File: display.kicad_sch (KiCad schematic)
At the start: 33 parts, among them J701 Socket_Molex_SlimStack_2x15_5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, J702 HDMI-A_WE_685119134923

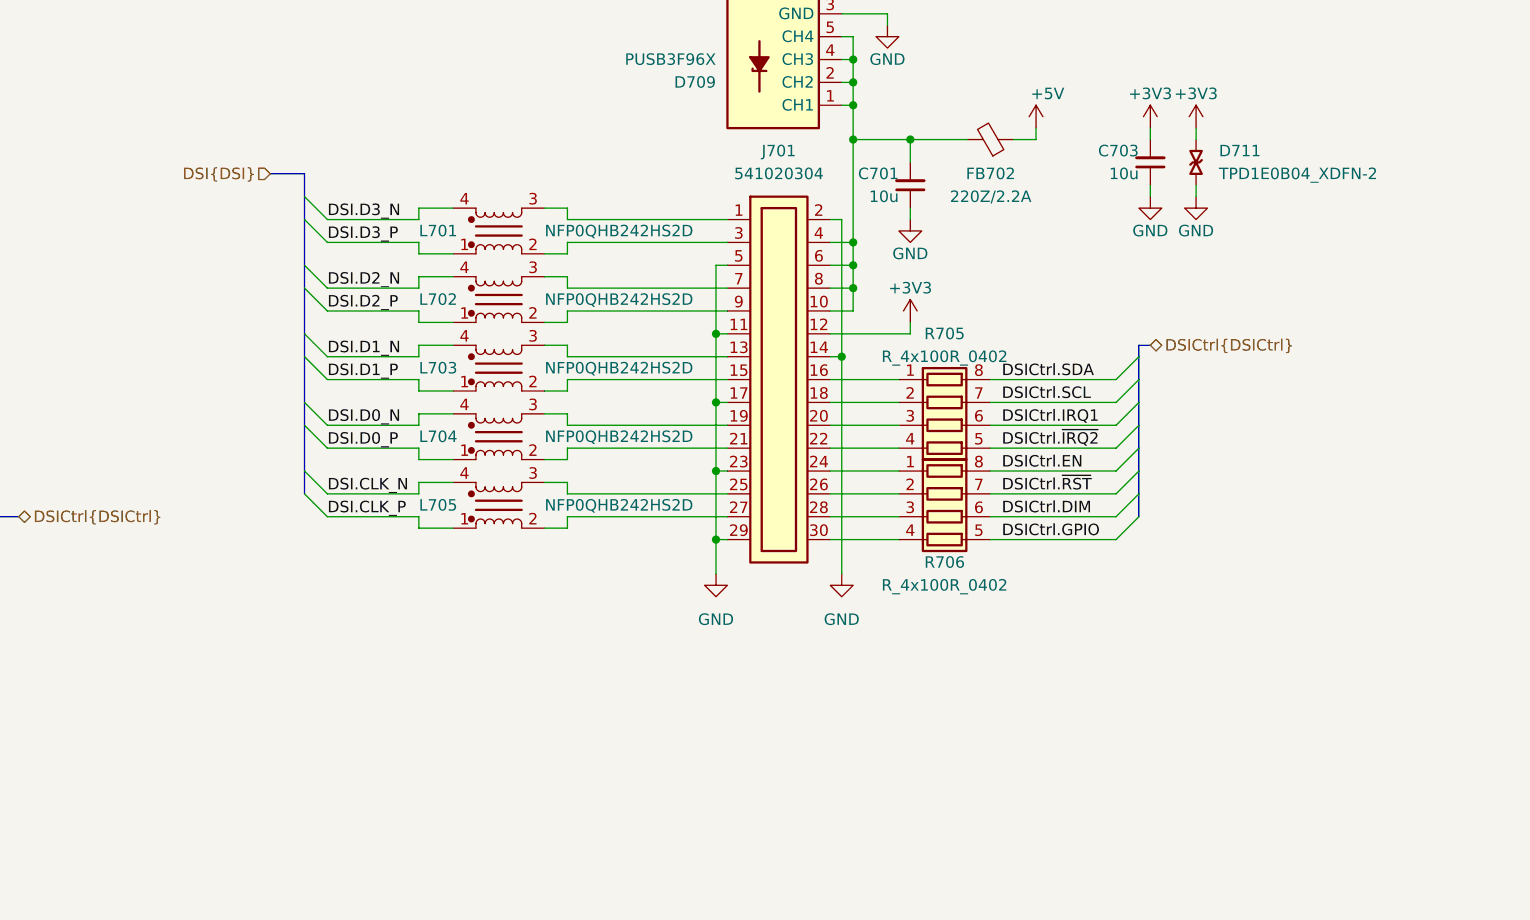
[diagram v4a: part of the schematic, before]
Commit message: [#54932] Change adapter connector (from 2x15 to 2x20)
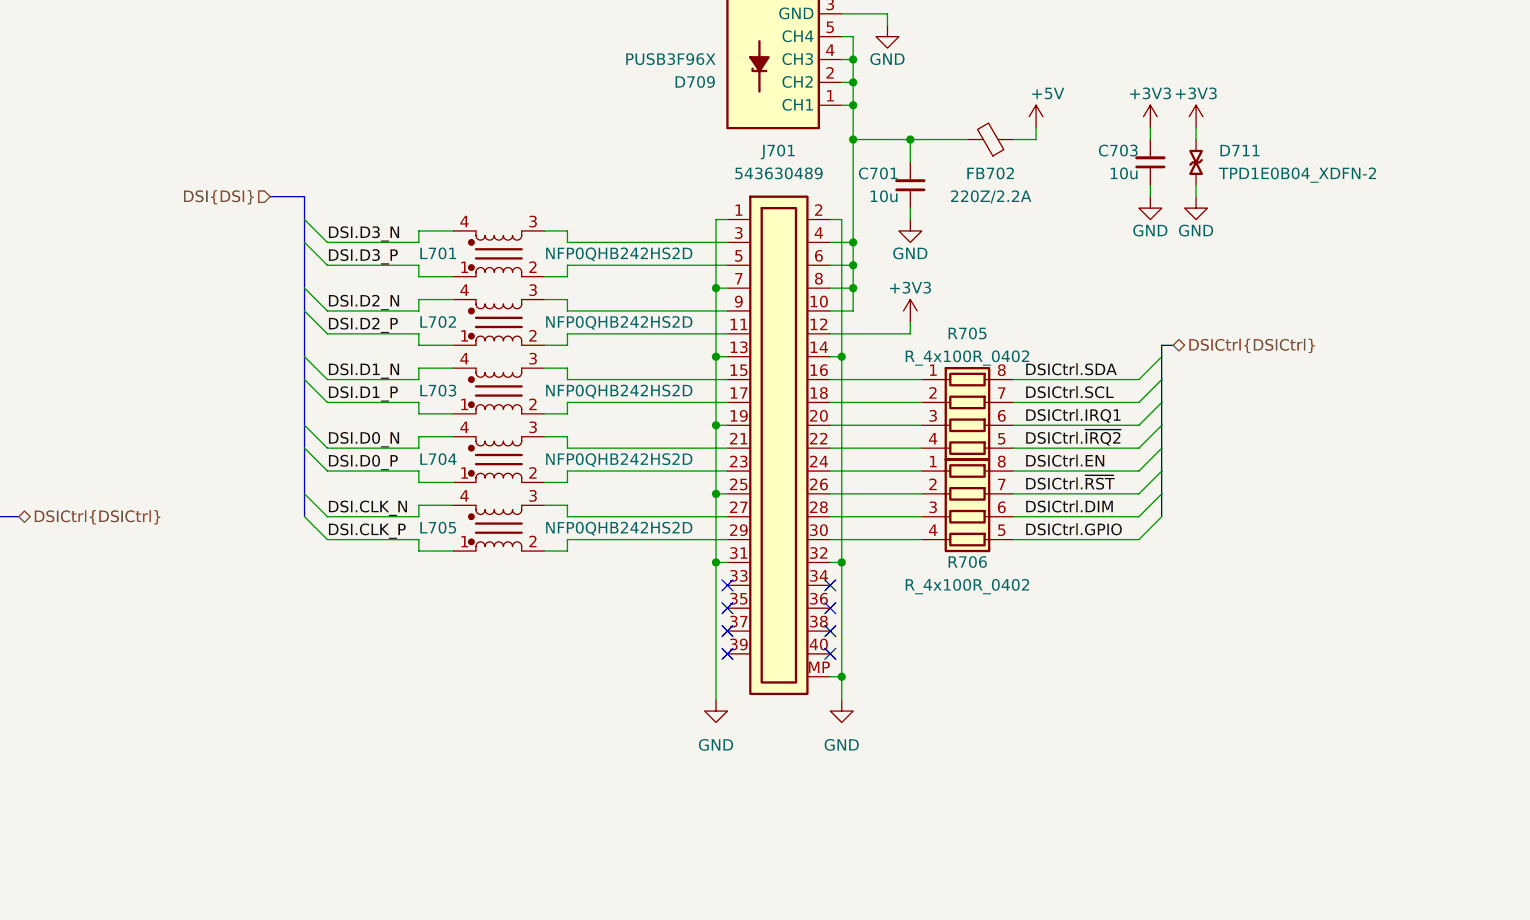
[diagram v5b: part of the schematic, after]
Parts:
- J701: value Socket_Molex_SlimStack_2x15_541020304 -> Socket_Molex_SlimStack_2x20_543630489; footprint antmicro-footprints:Conn_Socket_Molex_SlimStack_2x15_541020304 -> antmicro-footprints:Conn_Socket_Molex_SlimStack_2x20_543630489; symbol antmicroB2BConnectors:Socket_Molex_SlimStack_2x15_541020304 -> antmicroB2BConnectors:Socket_Molex_SlimStack_2x20_543630489; MPN 541020304 -> 543630489
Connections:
- net GND: now also J701.1, J701.13, J701.19, J701.25, J701.31, J701.32, J701.7, J701.MP; no longer J701.11, J701.17, J701.23, J701.29, J701.5
- net at L701.3: now also J701.3; no longer J701.1
- net at L703.3: now also J701.15; no longer J701.13
- net at L703.2: now also J701.17; no longer J701.15
- net at L704.3: now also J701.21; no longer J701.19
- net at L704.2: now also J701.23; no longer J701.21
- net at L705.3: now also J701.27; no longer J701.25
- net at L705.2: now also J701.29; no longer J701.27
- net at L701.2: now also J701.5; no longer J701.3
- net at L702.3: now also J701.9; no longer J701.7
- net at L702.2: now also J701.11; no longer J701.9
- no-connect marks 1 -> 9
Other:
- moved on the sheet: L701, L702, L703, L704, L705, R705, R706

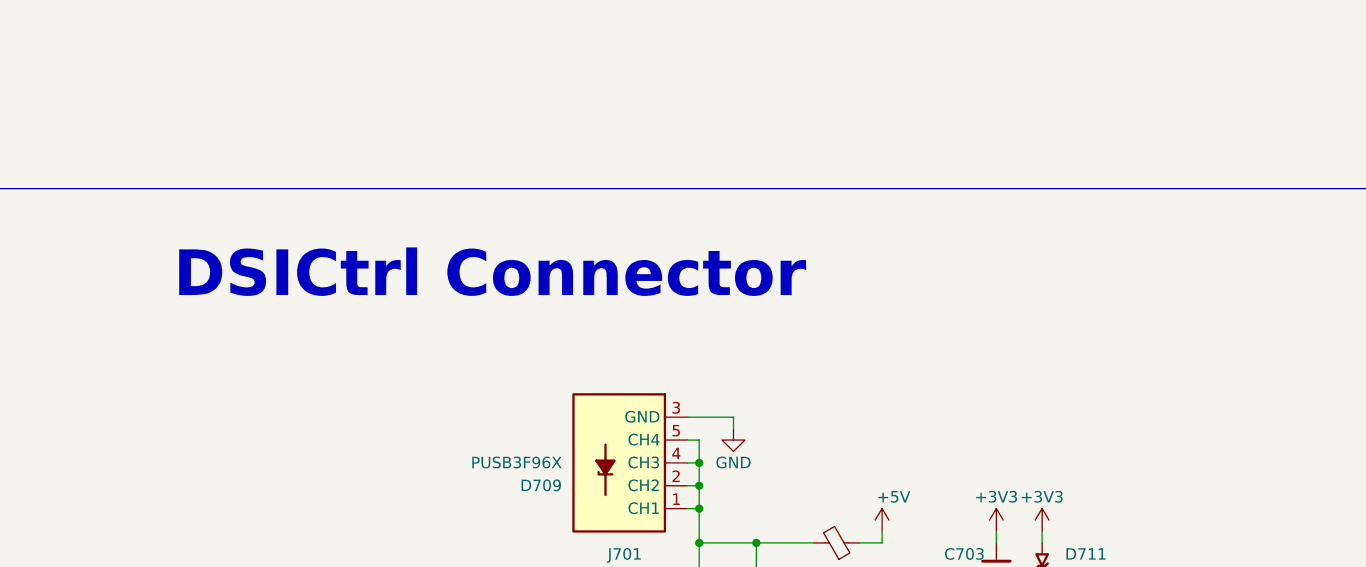
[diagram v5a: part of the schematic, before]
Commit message: [#54617] Change level shifter for I2C
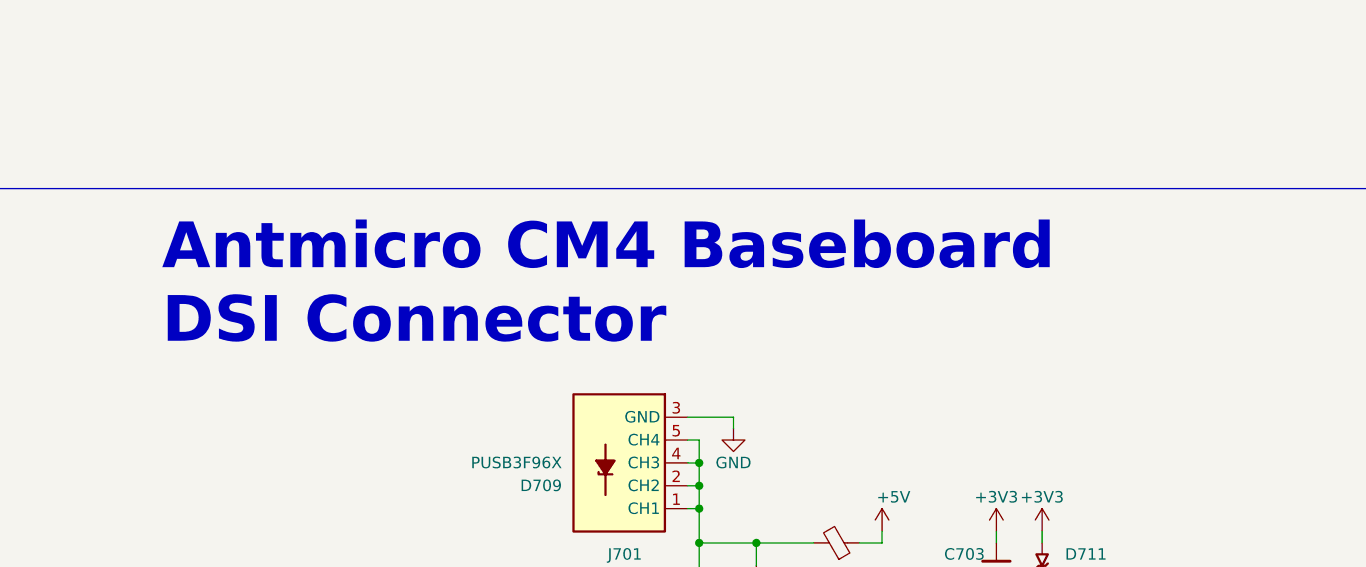
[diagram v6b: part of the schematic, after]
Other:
- note added: "Antmicro CM4 Baseboard DSI Connector"
- note removed: "DSICtrl Connector"
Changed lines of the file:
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@@
     (effects (font (size 5.08 5.08) (thickness 1.016) bold) (justify left bottom))
   )
-  (text "DSICtrl Connector" (at 177.8 147.32 0)
+  (text "Antmicro CM4 Baseboard \nDSI Connector" (at 176.53 152.4 0)
     (effects (font (size 5.08 5.08) (thickness 1.016) bold) (justify left bottom))
   )

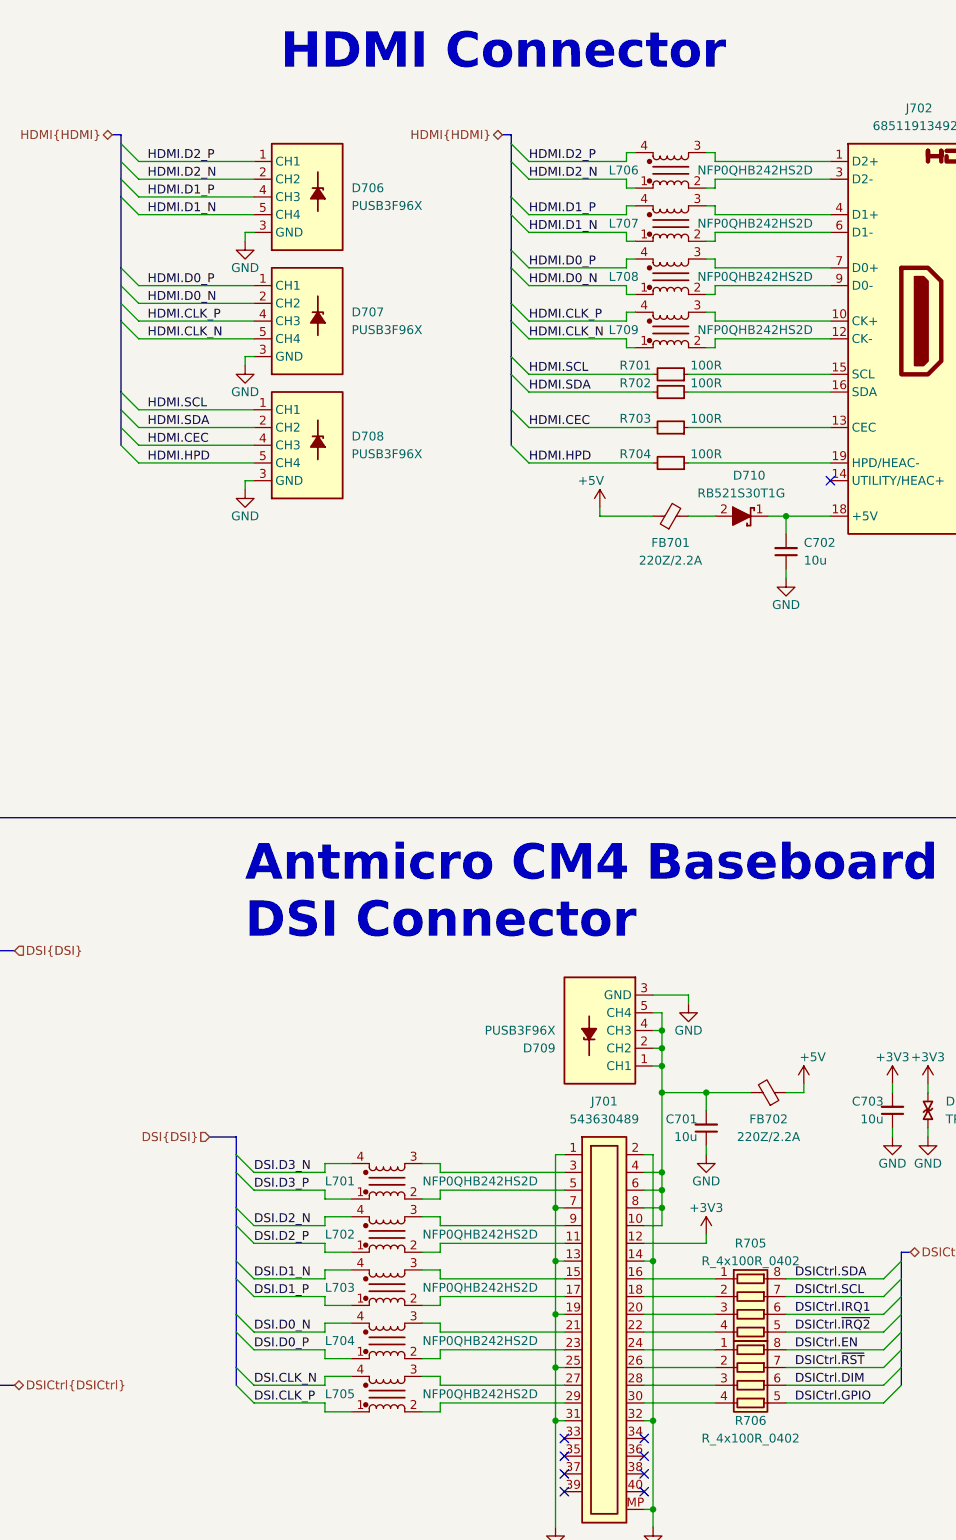
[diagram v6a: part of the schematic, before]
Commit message: [#54617] Remove CM chokes for HDMI & DSI; change CM chokes for USB
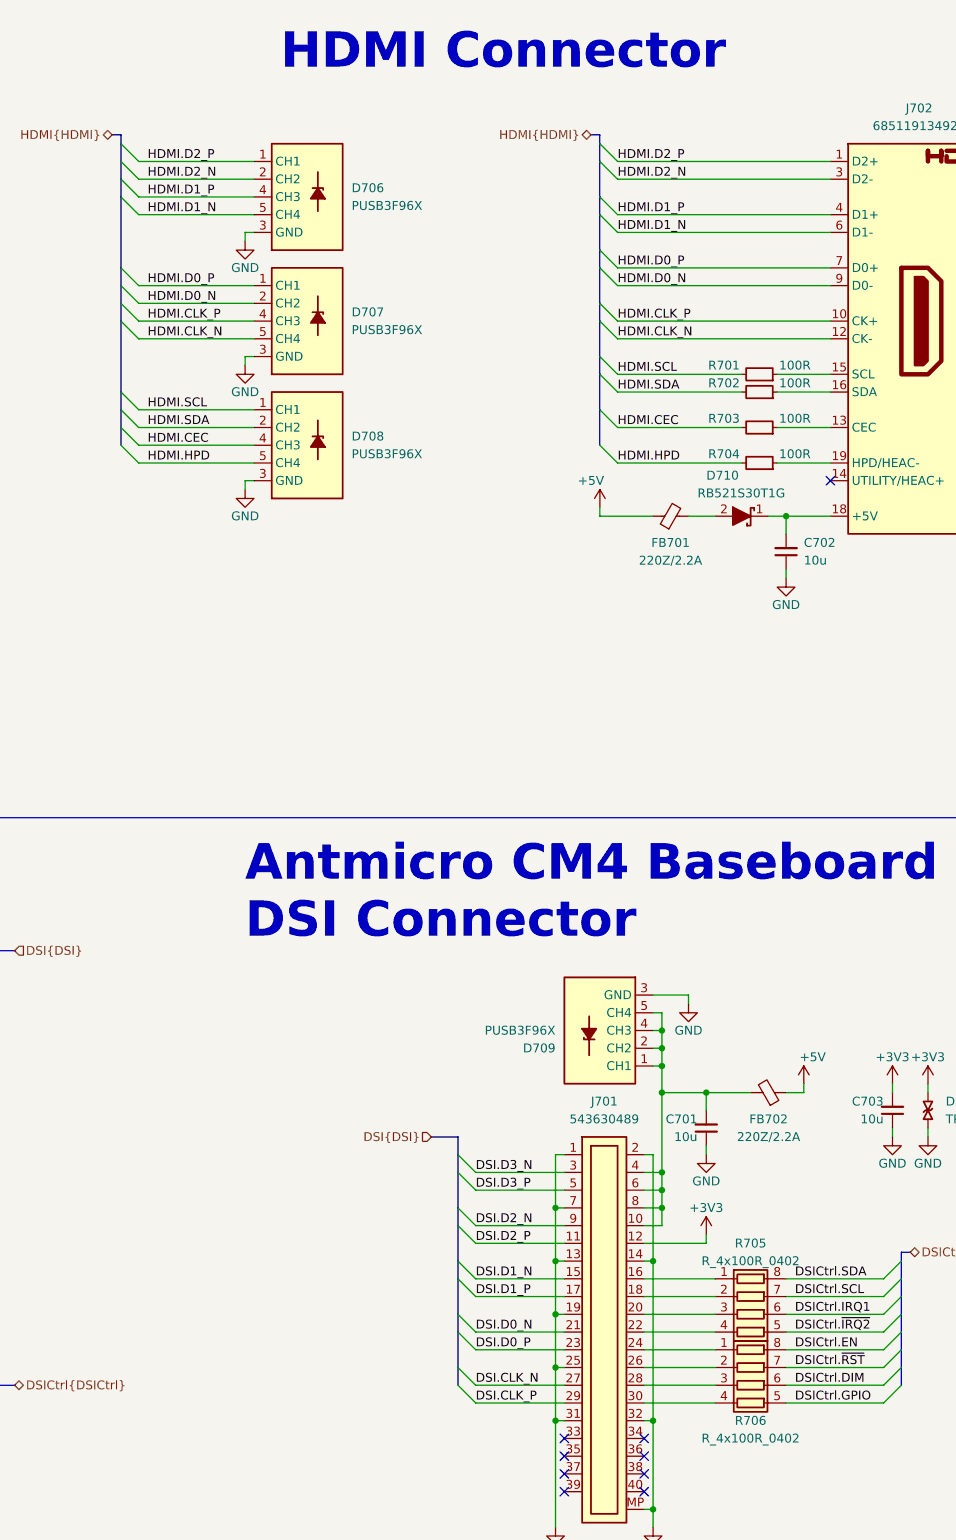
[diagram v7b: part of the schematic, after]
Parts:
- removed L701, L702, L703, L704, L705, L706, L707, L708, L709: NFP0QHB242HS2D, antmicro-footprints:Choke_025020_0605Metric, symbol antmicroCommonModeChokes:Choke_NFP0QHB242HS2D
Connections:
- net DSI.CLK_N: now also J701.27
- net DSI.CLK_P: now also J701.29
- net DSI.D0_N: now also J701.21
- net DSI.D0_P: now also J701.23
- net DSI.D1_N: now also J701.15
- net DSI.D1_P: now also J701.17
- net DSI.D2_N: now also J701.9
- net DSI.D2_P: now also J701.11
- net DSI.D3_N: now also J701.3
- net DSI.D3_P: now also J701.5
- net HDMI.CLK_N: now also J702.12 (CK-)
- net HDMI.CLK_P: now also J702.10 (CK+)
- net HDMI.D0_N: now also J702.9 (D0-)
- net HDMI.D0_P: now also J702.7 (D0+)
- net HDMI.D1_N: now also J702.6 (D1-)
- net HDMI.D1_P: now also J702.4 (D1+)
- net HDMI.D2_N: now also J702.3 (D2-)
- net HDMI.D2_P: now also J702.1 (D2+)
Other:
- moved on the sheet: R701, R702, R703, R704

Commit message: [#55181] PCB: PoE: Placement
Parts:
- J701: footprint antmicro-footprints:Conn_Socket_Molex_SlimStack_2x20_543630489 -> antmicro-footprints:Conn_Socket_Molex_SlimStack_2x20_529910408; symbol antmicroB2BConnectors:Socket_Molex_SlimStack_2x20_543630489 -> antmicroB2BConnectors:Socket_Molex_SlimStack_2x20_529910408; MPN 543630489 -> 529910408; Pitch  (none) -> 0.5 mm
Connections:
- net GND: no longer J701.MP
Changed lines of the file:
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@@
   (junction (at 236.22 190.5) (diameter 0) (color 0 0 0 0)
   )
-  (junction (at 234.95 233.68) (diameter 0) (color 0 0 0 0)
-  )
   (junction (at 287.02 88.9) (diameter 0) (color 0 0 0 0)
   )
@@
     (stroke (width 0) (type default))
   )
-  (wire (pts (xy 234.95 220.98) (xy 234.95 233.68))
+  (wire (pts (xy 234.95 220.98) (xy 234.95 236.22))
     (stroke (width 0) (type default))
   )
@@
     (stroke (width 0) (type default))
   )
-  (wire (pts (xy 233.68 233.68) (xy 234.95 233.68))
-    (stroke (width 0) (type default))
-  )
   (bus (pts (xy 140.97 222.25) (xy 140.97 224.79))
     (stroke (width 0) (type default))
@@
     (stroke (width 0) (type default))
   )
-  (wire (pts (xy 234.95 233.68) (xy 234.95 236.22))
-    (stroke (width 0) (type default))
-  )
   (bus (pts (xy 270.51 210.82) (xy 270.51 213.36))
     (stroke (width 0) (type default))
@@
     (effects (font (size 1.27 1.27)) (justify left))
   )
-  (symbol (lib_id "antmicroB2BConnectors:Socket_Molex_SlimStack_2x20_543630489") (at 222.25 182.88 0) (unit 1)
+  (symbol (lib_id "antmicroB2BConnectors:Socket_Molex_SlimStack_2x20_529910408") (at 222.25 182.88 0) (unit 1)
     (in_bom yes) (on_board yes) (dnp no) (fields_autoplaced)
     (property "Reference" "J701" (at 227.965 175.26 0)
@@
       (effects (font (size 1.27 1.27) (thickness 0.15)) (justify left bottom) hide)
     )
-    (property "Footprint" "antmicro-footprints:Conn_Socket_Molex_SlimStack_2x20_543630489" (at 247.65 190.5 0)
+    (property "Footprint" "antmicro-footprints:Conn_Socket_Molex_SlimStack_2x20_529910408" (at 247.65 190.5 0)
       (effects (font (size 1.27 1.27) (thickness 0.15)) (justify left bottom) hide)
     )
-    (property "Datasheet" "https://www.molex.com/pdm_docs/sd/543630489_sd.pdf" (at 247.65 193.04 0)
+    (property "Datasheet" "https://www.molex.com/en-us/products/part-detail/529910408?display=pdf" (at 247.65 193.04 0)
       (effects (font (size 1.27 1.27) (thickness 0.15)) (justify left bottom) hide)
     )
-    (property "MPN" "543630489" (at 227.965 177.8 0)
+    (property "MPN" "529910408" (at 227.965 177.8 0)
       (effects (font (size 1.27 1.27) (thickness 0.15)))
     )
-    (property "Manufacturer" "Molex" (at 247.65 198.12 0)
+    (property "Manufacturer" "Molex" (at 247.65 195.58 0)
       (effects (font (size 1.27 1.27) (thickness 0.15)) (justify left bottom) hide)
     )
@@
       (effects (font (size 1.27 1.27) (thickness 0.15)) (justify left bottom) hide)
     )
+    (property "Pitch " "0.5 mm" (at 247.65 198.12 0)
+      (effects (font (size 1.27 1.27)) (justify left bottom) hide)
+    )
     (pin "8")
     (pin "7")
@@
     (pin "40")
     (pin "37")
-    (pin "MP")
     (pin "38")
     (pin "32")
